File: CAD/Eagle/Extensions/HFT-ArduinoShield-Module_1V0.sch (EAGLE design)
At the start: 14 parts, among them X201 2X20/90_1MM27_HARWIN_M50-3902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, X202 2X20/90_1MM27_HARWIN_M50-3902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

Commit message: HW_ARDUINO - first try of layout
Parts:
- C108, C118: value (none) -> 100nF
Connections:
- net +3V3: now also X190.1, X190.2; no longer X190.3, X190.4
- net +5V0: now also X190.3, X190.4; no longer X190.5, X190.6
- net CLK_IN_N: now also X190.10, X190.9; no longer X190.11, X190.12
- net CLK_IN_P: now also X190.7, X190.8; no longer X190.10, X190.9
- net DCE_CTS_OUT: now also X190.23, X190.24
- net DCE_RTS_IN: now also X190.25, X190.26
- net DCE_RX_IN: now also X190.21, X190.22; no longer X190.23, X190.24
- net DCE_TX_OUT: now also X190.19, X190.20; no longer X190.21, X190.22
- net EVENT_IN: now also X190.13, X190.14; no longer X190.15, X190.16
- net GND: now also X190.11, X190.12, X190.5, X190.6; no longer X190.1, X190.13, X190.14, X190.2, X190.33, X190.34, X190.7, X190.8
- net P00: now also X190.27, X190.28; no longer X190.25, X190.26
- net P01: now also X190.29, X190.30; no longer X190.27, X190.28
- net P02: now also X190.31, X190.32; no longer X190.29, X190.30
- net P03: now also X190.33, X190.34; no longer X190.31, X190.32
- net TIMCAP_OUT: now also X190.15, X190.16; no longer X190.17, X190.18
- net WAKEUP_OUT: now also X190.17, X190.18; no longer X190.19, X190.20

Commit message: HW_ARDUINO - Raspberry Pi socket added, also
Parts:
- removed H301, H302, H303, H304: MOUNT-PAD-ROUND2.8, holes:MOUNT-PAD-ROUND2.8
- removed X202: 2X20/90_1MM27_HARWIN_M50-3902042_HEADER, df4iah_connector:2X20/90_1MM27_HARWIN_M50-3902042_HEADER
- added H401, H402, H403, H404: MOUNT-PAD-ROUND2.8, holes:MOUNT-PAD-ROUND2.8
- added R110: 47R, df4iah_rcl:R-EU_R0603
- added R201: 120R, df4iah_rcl:R-EU_R0603
- added X301, X302: 2X20/90_1MM27_HARWIN_M50-3902042_HEADER, df4iah_connector:2X20/90_1MM27_HARWIN_M50-3902042_HEADER
- X201: value 2X20/90_1MM27_HARWIN_M50-3902042_HEADER -> (none); device df4iah_connector:2X20/90_1MM27_HARWIN_M50-3902042_HEADER -> df4iah_connector:2X20_2MM56_SOCKET
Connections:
- removed net N107_11: R107.1, X107.11, X107.12
- removed net N110_13: X110.13, X110.14
- removed net N110_15: X110.15, X110.16
- new net DCE_TX_OUT_R: R110.1, X110.13, X110.14, X190.19, X190.20, X201.8
- new net SPI_MISO_OUT_R: R107.1, X107.11, X107.12, X201.21, X201.35
- net +3V3: now also X201.1, X201.17, X301.3, X301.4, X302.37, X302.38; no longer X201.3, X201.4, X202.37, X202.38
- net +5V0: now also X201.2, X201.4, X301.37, X301.38; no longer X201.37, X201.38
- net CLK_IN_N: now also R201.1, X302.4; no longer X202.4
- net CLK_IN_P: now also R201.2, X201.7, X302.3; no longer X202.3
- net DCE_CTS_OUT: now also X301.26; no longer X201.26
- net DCE_RTS_IN: now also X301.25; no longer X201.25
- net DCE_RX_IN: now also X110.15, X110.16, X201.10, X301.23; no longer X201.23
- net DCE_TX_OUT: now also R110.2, X301.24; no longer X190.19, X190.20, X201.24
- net EVENT_IN: now also X301.29; no longer X201.29
- net GND: now also H401.MOUNT, H402.MOUNT, H403.MOUNT, H404.MOUNT, X201.20, X201.25, X201.9, X301.1, X301.10, X301.12, X301.14, X301.2, X301.21, X301.22, X301.27, X301.28, X301.30, X301.32, X301.34, X301.35, X301.36, X301.39, X301.40, X301.5, X301.6, X301.8, X302.1, X302.10, X302.14, X302.15, X302.16, X302.2, X302.21, X302.22, X302.25, X302.27, X302.28, X302.39, X302.40, X302.5, X302.6, X302.9; no longer H301.MOUNT, H302.MOUNT, H303.MOUNT, H304.MOUNT, X201.1, X201.10, X201.12, X201.2, X201.21, X201.22, X201.27, X201.28, X201.32, X201.35, X201.36, X201.40, X201.5, X201.8, X202.1, X202.10, X202.14, X202.15, X202.16, X202.2, X202.21, X202.22, X202.25, X202.27, X202.28, X202.39, X202.40, X202.5, X202.6, X202.9
- net I2C_SCL_IN: now also X201.5, X302.7; no longer X202.7
- net I2C_SDA_INOUT: now also X201.3, X302.8; no longer X202.8
- net I2S_A_FS_IN: now also X302.20; no longer X202.20
- net I2S_A_MCLK_IN: now also X302.19; no longer X202.19
- net I2S_A_SCK_IN: now also X302.17; no longer X202.17
- net I2S_A_SD_IN: now also X302.18; no longer X202.18
- net I2S_B_FS_OUT: now also X302.26; no longer X202.26
- net I2S_B_SCK_OUT: now also X302.23; no longer X202.23
- net I2S_B_SD_OUT: now also X302.24; no longer X202.24
- net P00: now also X201.24, X301.7; no longer X201.7
- net P01: now also X201.26, X301.9; no longer X201.9
- net P02: now also X201.12, X201.32, X301.11; no longer X201.11
- net P03: now also X201.33, X301.13; no longer X201.13
- net SPI_MISO_OUT: now also X302.12; no longer X202.12
- net SPI_MOSI_IN: now also X201.19, X201.38, X302.11; no longer X202.11
- net SPI_SCK_IN: now also X201.23, X201.40, X302.13; no longer X202.13
- net TIMCAP_OUT: now also X301.31; no longer X201.31
- net WAKEUP_OUT: now also X301.33; no longer X201.33
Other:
- note added: "(RXD)"
- note added: "(TXD)"
- note added: "Arduino Uno sockets"
- note added: "Board & mounting holes"
- note added: "Expansion connectors to the HFT-Core-Module"
- note added: "Raspberry Pi socket"
- note removed: "Board"
- note removed: "Mounting holes"

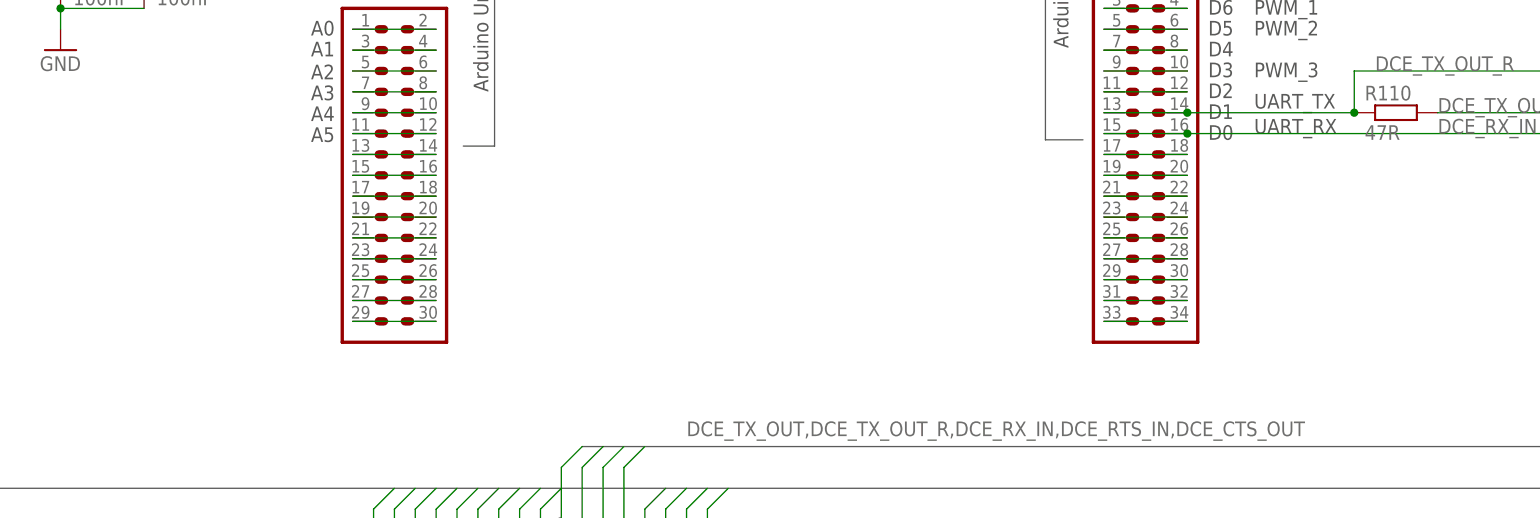
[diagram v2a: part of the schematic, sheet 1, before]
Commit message: HW_ARDUINO - Interconnect between PI socket and Arduino sockets added
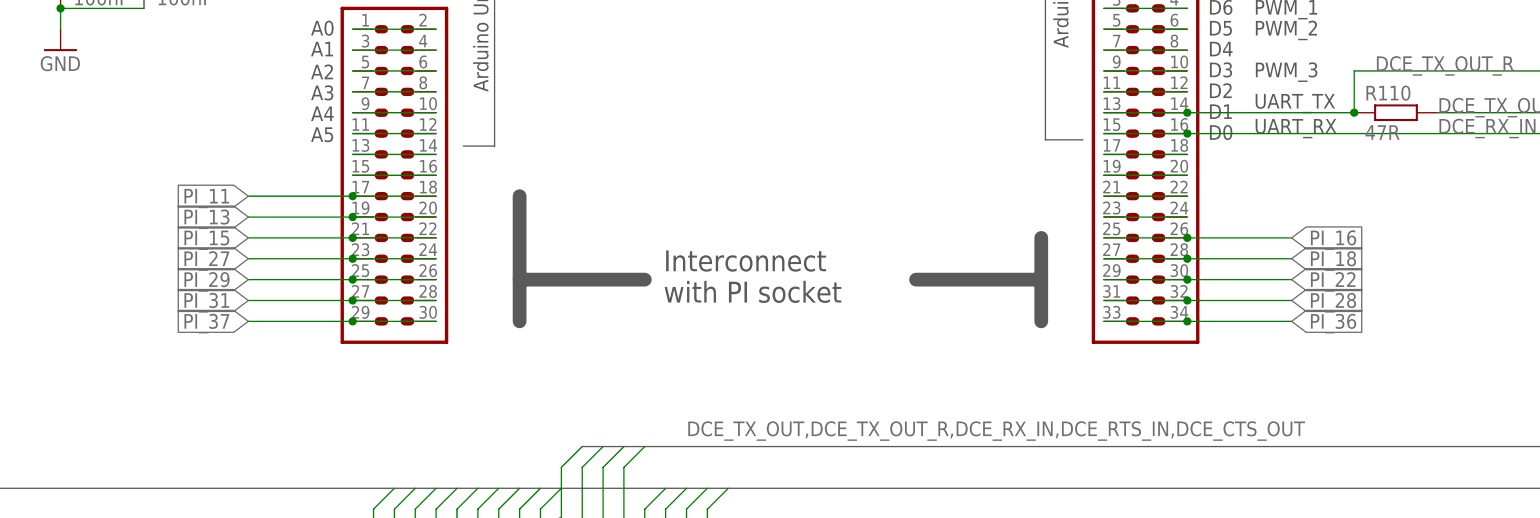
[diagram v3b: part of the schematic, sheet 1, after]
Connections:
- removed net N105_17: X105.17, X105.18
- removed net N105_19: X105.19, X105.20
- removed net N105_21: X105.21, X105.22
- removed net N105_23: X105.23, X105.24
- removed net N105_25: X105.25, X105.26
- removed net N105_27: X105.27, X105.28
- removed net N105_29: X105.29, X105.30
- removed net N110_25: X110.25, X110.26
- removed net N110_27: X110.27, X110.28
- removed net N110_29: X110.29, X110.30
- removed net N110_31: X110.31, X110.32
- removed net N110_33: X110.33, X110.34
- new net PI_11: X105.17, X105.18, X201.11
- new net PI_13: X105.19, X105.20, X201.13
- new net PI_15: X105.21, X105.22, X201.15
- new net PI_16: X110.25, X110.26, X201.16
- new net PI_18: X110.27, X110.28, X201.18
- new net PI_22: X110.29, X110.30, X201.22
- new net PI_27: X105.23, X105.24, X201.27
- new net PI_28: X110.31, X110.32, X201.28
- new net PI_29: X105.25, X105.26, X201.29
- new net PI_31: X105.27, X105.28, X201.31
- new net PI_36: X110.33, X110.34, X201.36
- new net PI_37: X105.29, X105.30, X201.37
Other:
- note added: "Interconnect with Arduino sockets: PI_xx"
- note added: "Interconnect with PI socket"
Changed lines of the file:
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@@
 <text x="175.26" y="88.138" size="1.778" layer="97">D0</text>
 <text x="22.86" y="162.56" size="2.54" layer="97" ratio="15">Arduino Uno sockets</text>
+<text x="108.966" y="68.326" size="2.54" layer="97">Interconnect
+with PI socket</text>
+<wire x1="91.44" y1="71.12" x2="106.68" y2="71.12" width="1.6764" layer="97"/>
+<wire x1="139.7" y1="71.12" x2="154.94" y2="71.12" width="1.6764" layer="97"/>
+<wire x1="91.44" y1="81.28" x2="91.44" y2="66.04" width="1.6764" layer="97"/>
+<wire x1="154.94" y1="76.2" x2="154.94" y2="66.04" width="1.6764" layer="97"/>
 </plain>
 <instances>
@@
 </segment>
 </net>
-<net name="N105_17" class="0">
+<net name="PI_11" class="0">
 <segment>
 <pinref part="X105" gate="G$1" pin="17"/>
 <pinref part="X105" gate="G$1" pin="18"/>
 <wire x1="71.12" y1="81.28" x2="81.28" y2="81.28" width="0.1524" layer="91"/>
-</segment>
-</net>
-<net name="N105_19" class="0">
+<wire x1="71.12" y1="81.28" x2="58.42" y2="81.28" width="0.1524" layer="91"/>
+<junction x="71.12" y="81.28"/>
+<label x="58.42" y="81.28" size="1.778" layer="95" rot="R180" xref="yes"/>
+</segment>
+</net>
+<net name="PI_13" class="0">
 <segment>
 <pinref part="X105" gate="G$1" pin="19"/>
 <pinref part="X105" gate="G$1" pin="20"/>
 <wire x1="71.12" y1="78.74" x2="81.28" y2="78.74" width="0.1524" layer="91"/>
-</segment>
-</net>
-<net name="N105_21" class="0">
+<wire x1="71.12" y1="78.74" x2="58.42" y2="78.74" width="0.1524" layer="91"/>
+<junction x="71.12" y="78.74"/>
+<label x="58.42" y="78.74" size="1.778" layer="95" rot="R180" xref="yes"/>
+</segment>
+</net>
+<net name="PI_15" class="0">
 <segment>
 <pinref part="X105" gate="G$1" pin="21"/>
 <pinref part="X105" gate="G$1" pin="22"/>
 <wire x1="71.12" y1="76.2" x2="81.28" y2="76.2" width="0.1524" layer="91"/>
-</segment>
-</net>
-<net name="N105_23" class="0">
+<wire x1="71.12" y1="76.2" x2="58.42" y2="76.2" width="0.1524" layer="91"/>
+<junction x="71.12" y="76.2"/>
+<label x="58.42" y="76.2" size="1.778" layer="95" rot="R180" xref="yes"/>
+</segment>
+</net>
+<net name="PI_27" class="0">
 <segment>
 <pinref part="X105" gate="G$1" pin="23"/>
 <pinref part="X105" gate="G$1" pin="24"/>
 <wire x1="71.12" y1="73.66" x2="81.28" y2="73.66" width="0.1524" layer="91"/>
-</segment>
-</net>
-<net name="N105_25" class="0">
+<wire x1="71.12" y1="73.66" x2="58.42" y2="73.66" width="0.1524" layer="91"/>
+<junction x="71.12" y="73.66"/>
+<label x="58.42" y="73.66" size="1.778" layer="95" rot="R180" xref="yes"/>
+</segment>
+</net>
+<net name="PI_29" class="0">
 <segment>
 <pinref part="X105" gate="G$1" pin="25"/>
 <pinref part="X105" gate="G$1" pin="26"/>
 <wire x1="71.12" y1="71.12" x2="81.28" y2="71.12" width="0.1524" layer="91"/>
-</segment>
-</net>
-<net name="N105_27" class="0">
+<wire x1="71.12" y1="71.12" x2="58.42" y2="71.12" width="0.1524" layer="91"/>
+<junction x="71.12" y="71.12"/>
+<label x="58.42" y="71.12" size="1.778" layer="95" rot="R180" xref="yes"/>
+</segment>
+</net>
+<net name="PI_31" class="0">
 <segment>
 <pinref part="X105" gate="G$1" pin="27"/>
 <pinref part="X105" gate="G$1" pin="28"/>
 <wire x1="71.12" y1="68.58" x2="81.28" y2="68.58" width="0.1524" layer="91"/>
-</segment>
-</net>
-<net name="N105_29" class="0">
+<wire x1="71.12" y1="68.58" x2="58.42" y2="68.58" width="0.1524" layer="91"/>
+<junction x="71.12" y="68.58"/>
+<label x="58.42" y="68.58" size="1.778" layer="95" rot="R180" xref="yes"/>
+</segment>
+</net>
+<net name="PI_37" class="0">
 <segment>
 <pinref part="X105" gate="G$1" pin="29"/>
 <pinref part="X105" gate="G$1" pin="30"/>
 <wire x1="71.12" y1="66.04" x2="81.28" y2="66.04" width="0.1524" layer="91"/>
+<wire x1="71.12" y1="66.04" x2="58.42" y2="66.04" width="0.1524" layer="91"/>
+<junction x="71.12" y="66.04"/>
+<label x="58.42" y="66.04" size="1.778" layer="95" rot="R180" xref="yes"/>
 </segment>
 </net>
@@
 </segment>
 </net>
-<net name="N110_25" class="0">
+<net name="PI_16" class="0">
 <segment>
 <pinref part="X110" gate="G$1" pin="25"/>
 <pinref part="X110" gate="G$1" pin="26"/>
 <wire x1="162.56" y1="76.2" x2="172.72" y2="76.2" width="0.1524" layer="91"/>
-</segment>
-</net>
-<net name="N110_27" class="0">
+<wire x1="172.72" y1="76.2" x2="185.42" y2="76.2" width="0.1524" layer="91"/>
+<junction x="172.72" y="76.2"/>
+<label x="185.42" y="76.2" size="1.778" layer="95" xref="yes"/>
+</segment>
+</net>
+<net name="PI_18" class="0">
 <segment>
 <pinref part="X110" gate="G$1" pin="27"/>
 <pinref part="X110" gate="G$1" pin="28"/>
 <wire x1="162.56" y1="73.66" x2="172.72" y2="73.66" width="0.1524" layer="91"/>
-</segment>
-</net>
-<net name="N110_29" class="0">
+<wire x1="172.72" y1="73.66" x2="185.42" y2="73.66" width="0.1524" layer="91"/>
+<junction x="172.72" y="73.66"/>
+<label x="185.42" y="73.66" size="1.778" layer="95" xref="yes"/>
+</segment>
+</net>
+<net name="PI_22" class="0">
 <segment>
 <pinref part="X110" gate="G$1" pin="29"/>
 <pinref part="X110" gate="G$1" pin="30"/>
 <wire x1="162.56" y1="71.12" x2="172.72" y2="71.12" width="0.1524" layer="91"/>
-</segment>
-</net>
-<net name="N110_31" class="0">
+<wire x1="172.72" y1="71.12" x2="185.42" y2="71.12" width="0.1524" layer="91"/>
+<junction x="172.72" y="71.12"/>
+<label x="185.42" y="71.12" size="1.778" layer="95" xref="yes"/>
+</segment>
+</net>
+<net name="PI_28" class="0">
 <segment>
 <pinref part="X110" gate="G$1" pin="31"/>
 <pinref part="X110" gate="G$1" pin="32"/>
 <wire x1="162.56" y1="68.58" x2="172.72" y2="68.58" width="0.1524" layer="91"/>
-</segment>
-</net>
-<net name="N110_33" class="0">
+<wire x1="172.72" y1="68.58" x2="185.42" y2="68.58" width="0.1524" layer="91"/>
+<junction x="172.72" y="68.58"/>
+<label x="185.42" y="68.58" size="1.778" layer="95" xref="yes"/>
+</segment>
+</net>
+<net name="PI_36" class="0">
 <segment>
 <pinref part="X110" gate="G$1" pin="33"/>
 <pinref part="X110" gate="G$1" pin="34"/>
 <wire x1="162.56" y1="66.04" x2="172.72" y2="66.04" width="0.1524" layer="91"/>
+<wire x1="172.72" y1="66.04" x2="185.42" y2="66.04" width="0.1524" layer="91"/>
+<junction x="172.72" y="66.04"/>
+<label x="185.42" y="66.04" size="1.778" layer="95" xref="yes"/>
 </segment>
 </net>
@@
 <text x="137.16" y="127" size="1.778" layer="97">(TXD)</text>
 <text x="137.16" y="124.46" size="1.778" layer="97">(RXD)</text>
+<text x="113.284" y="69.596" size="2.54" layer="97">Interconnect with
+Arduino sockets:
+PI_xx</text>
 </plain>
 <instances>
@@
 <wire x1="17.78" y1="119.38" x2="66.04" y2="119.38" width="0.1524" layer="91"/>
 <pinref part="R201" gate="G$1" pin="1"/>
+</segment>
+</net>
+<net name="PI_11" class="0">
+<segment>
+<pinref part="X201" gate="G$1" pin="11"/>
+<wire x1="124.46" y1="121.92" x2="111.76" y2="121.92" width="0.1524" layer="91"/>
+<label x="111.76" y="121.92" size="1.778" layer="95" rot="R180" xref="yes"/>
+</segment>
+</net>
+<net name="PI_13" class="0">
+<segment>
+<pinref part="X201" gate="G$1" pin="13"/>
+<wire x1="124.46" y1="119.38" x2="111.76" y2="119.38" width="0.1524" layer="91"/>
+<label x="111.76" y="119.38" size="1.778" layer="95" rot="R180" xref="yes"/>
+</segment>
+</net>
+<net name="PI_15" class="0">
+<segment>
+<pinref part="X201" gate="G$1" pin="15"/>
+<wire x1="124.46" y1="116.84" x2="111.76" y2="116.84" width="0.1524" layer="91"/>
+<label x="111.76" y="116.84" size="1.778" layer="95" rot="R180" xref="yes"/>
+</segment>
+</net>
+<net name="PI_27" class="0">
+<segment>
+<pinref part="X201" gate="G$1" pin="27"/>
+<wire x1="124.46" y1="101.6" x2="111.76" y2="101.6" width="0.1524" layer="91"/>
+<label x="111.76" y="101.6" size="1.778" layer="95" rot="R180" xref="yes"/>
+</segment>
+</net>
+<net name="PI_29" class="0">
+<segment>
+<pinref part="X201" gate="G$1" pin="29"/>
+<wire x1="124.46" y1="99.06" x2="111.76" y2="99.06" width="0.1524" layer="91"/>
+<label x="111.76" y="99.06" size="1.778" layer="95" rot="R180" xref="yes"/>
+</segment>
+</net>
+<net name="PI_31" class="0">
+<segment>
+<pinref part="X201" gate="G$1" pin="31"/>
+<wire x1="124.46" y1="96.52" x2="111.76" y2="96.52" width="0.1524" layer="91"/>
+<label x="111.76" y="96.52" size="1.778" layer="95" rot="R180" xref="yes"/>
+</segment>
+</net>
+<net name="PI_37" class="0">
+<segment>
+<pinref part="X201" gate="G$1" pin="37"/>
+<wire x1="124.46" y1="88.9" x2="111.76" y2="88.9" width="0.1524" layer="91"/>
+<label x="111.76" y="88.9" size="1.778" layer="95" rot="R180" xref="yes"/>
+</segment>
+</net>
+<net name="PI_16" class="0">
+<segment>
+<pinref part="X201" gate="G$1" pin="16"/>
+<wire x1="134.62" y1="116.84" x2="147.32" y2="116.84" width="0.1524" layer="91"/>
+<label x="147.32" y="116.84" size="1.778" layer="95" xref="yes"/>
+</segment>
+</net>
+<net name="PI_18" class="0">
+<segment>
+<pinref part="X201" gate="G$1" pin="18"/>
+<wire x1="134.62" y1="114.3" x2="147.32" y2="114.3" width="0.1524" layer="91"/>
+<label x="147.32" y="114.3" size="1.778" layer="95" xref="yes"/>
+</segment>
+</net>
+<net name="PI_22" class="0">
+<segment>
+<pinref part="X201" gate="G$1" pin="22"/>
+<wire x1="134.62" y1="109.22" x2="147.32" y2="109.22" width="0.1524" layer="91"/>
+<label x="147.32" y="109.22" size="1.778" layer="95" xref="yes"/>
+</segment>
+</net>
+<net name="PI_28" class="0">
+<segment>
+<pinref part="X201" gate="G$1" pin="28"/>
+<wire x1="134.62" y1="101.6" x2="147.32" y2="101.6" width="0.1524" layer="91"/>
+<label x="147.32" y="101.6" size="1.778" layer="95" xref="yes"/>
+</segment>
+</net>
+<net name="PI_36" class="0">
+<segment>
+<pinref part="X201" gate="G$1" pin="36"/>
+<wire x1="134.62" y1="91.44" x2="147.32" y2="91.44" width="0.1524" layer="91"/>
+<label x="147.32" y="91.44" size="1.778" layer="95" xref="yes"/>
 </segment>
 </net>
@@
 </schematic>
 </drawing>
+<compatibility>
+<note version="6.3" minversion="6.2.2" severity="warning">
+Since Version 6.2.2 text objects can contain more than one line,
+which will not be processed correctly with this version.
+</note>
+</compatibility>
 </eagle>
